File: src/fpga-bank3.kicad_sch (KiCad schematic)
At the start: 21 parts

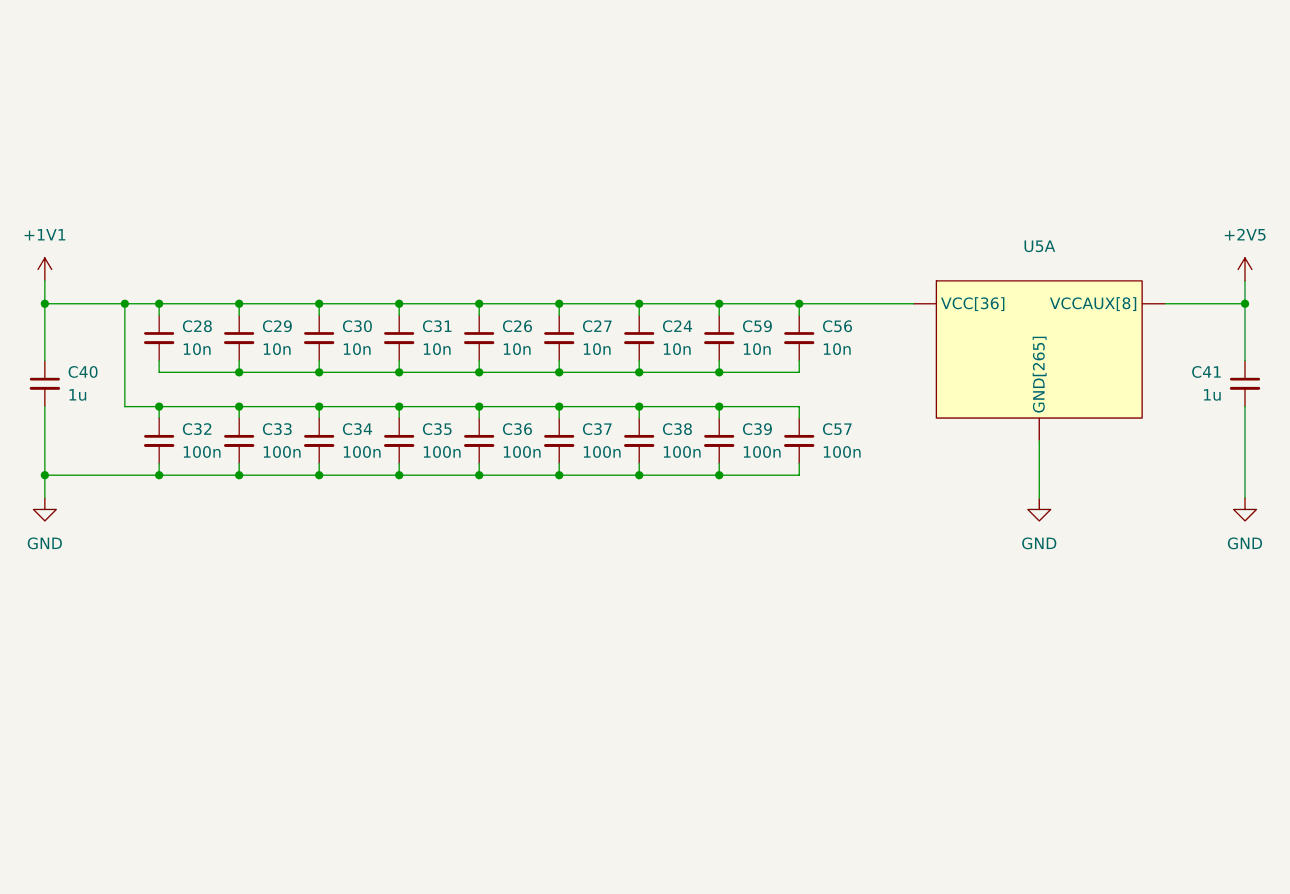
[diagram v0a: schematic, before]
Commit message: Adds more FPGA IO banks
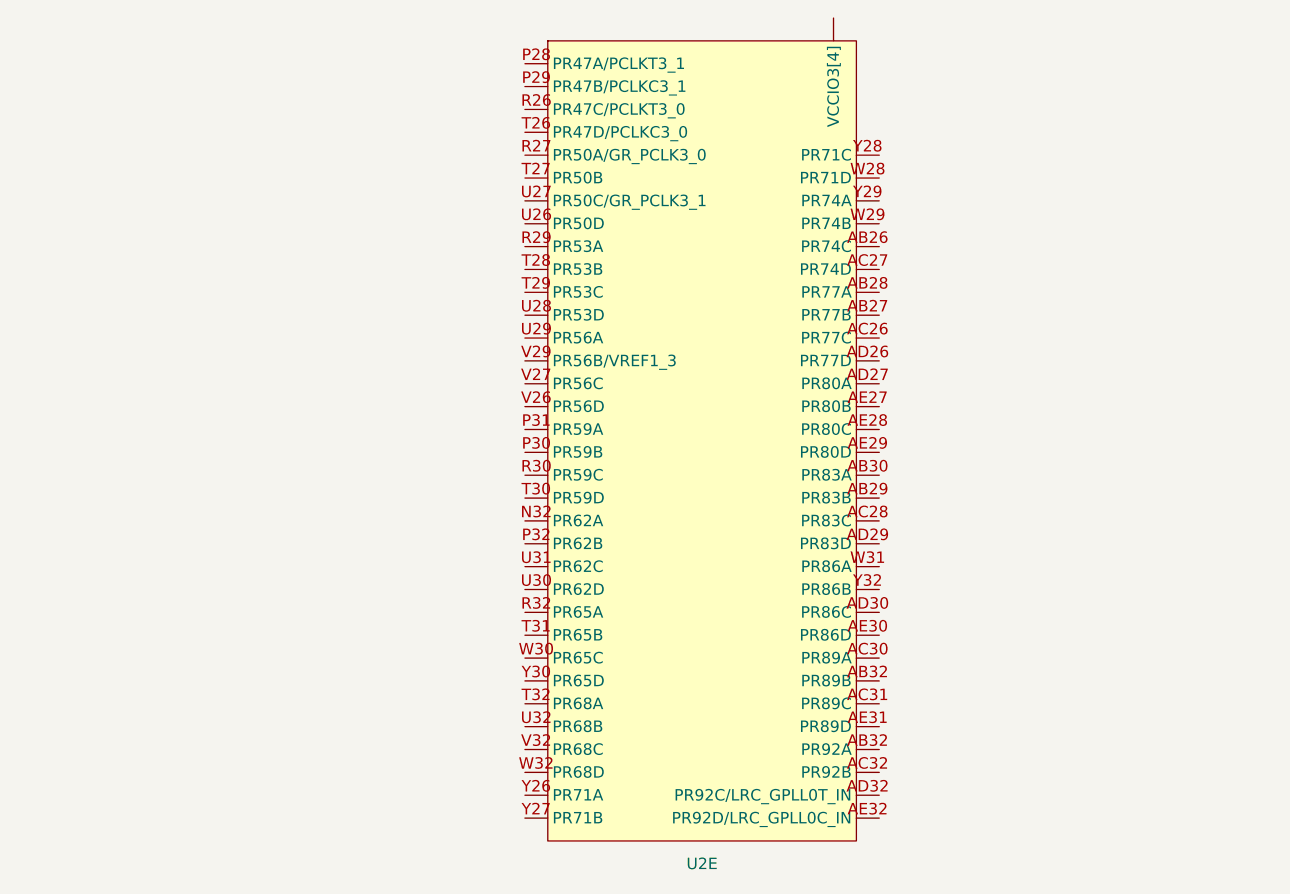
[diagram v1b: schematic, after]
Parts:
- removed C24, C26, C27, C28, C29, C30, C31, C56, C59: 10n, symbol Device:C_Small
- removed C32, C33, C34, C35, C36, C37, C38, C39, C57: 100n, symbol Device:C_Small
- removed C40, C41: 1u, symbol Device:C_Small
- removed U5: ~, symbol ECAP5-BSOM:LFE5U-85F-*BG756*
- added U2: ~, symbol ECAP5-BSOM:LFE5U-85F-*BG756*
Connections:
- new net VCCIO3: U2. (VCCIO3[4]), U2.AA23 (VCCIO3), U2.U23 (VCCIO3), U2.V23 (VCCIO3), U2.W23 (VCCIO3)
